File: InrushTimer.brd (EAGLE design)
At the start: 62.2 x 36 mm, 72 parts, among them IC1 TLC272D, IC2 555, IC3 4076N, Q1 TIP41C, Q2 TRANSISTOR-FET_2N7002, Q3 TRANSISTOR-FET_2N7002, Q4 TRANSISTOR-FET_2N7002, Q5 TRANSISTOR-FET_2N7002, T1 MMBTA05, U1 ROHM_BY_ELEMENT14_BATCH_1_BU4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

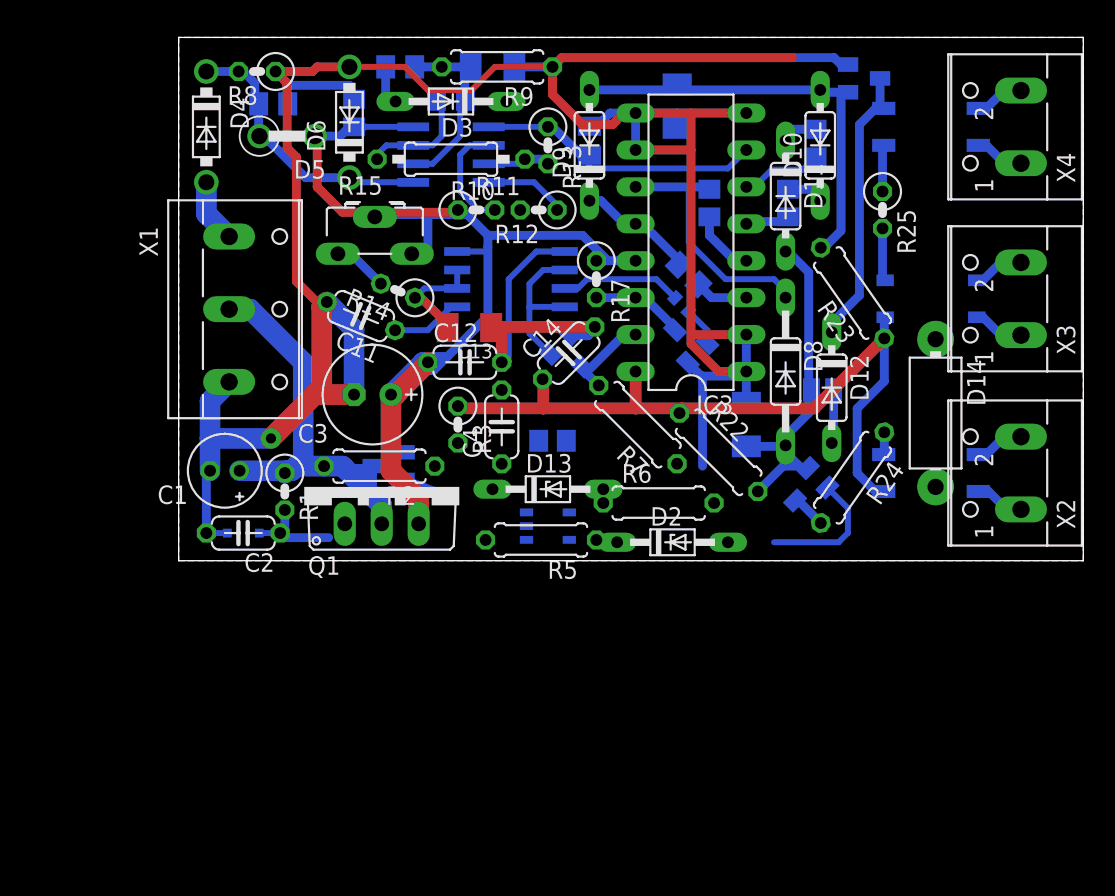
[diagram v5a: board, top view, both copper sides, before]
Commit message: Rerouted power supply section and made some space around the pot.
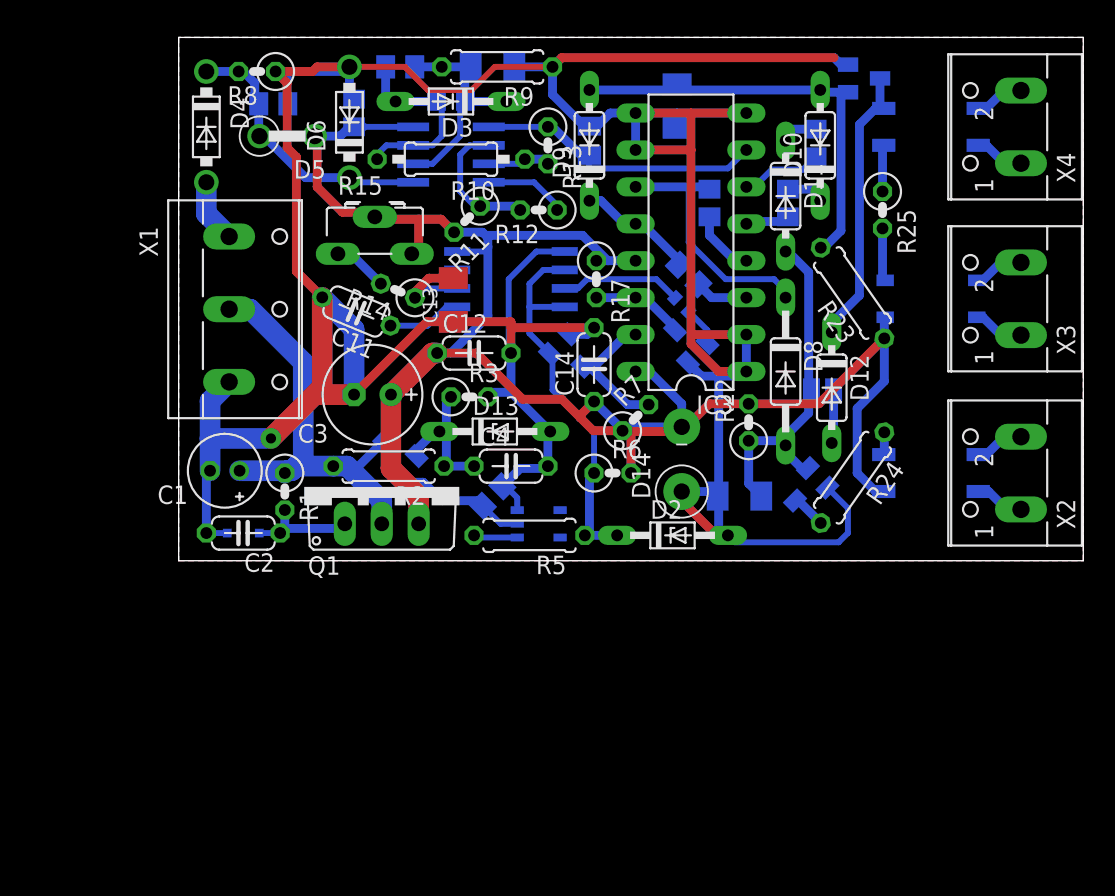
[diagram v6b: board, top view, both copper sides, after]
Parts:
- D14: value P6KEXXCTS-P6KE -> P6KEXXCDO15-10V; device diode:DO15-10 -> diode:DO15-10V
- R22, R6, R7: device rcl:0207/7 -> rcl:0207/2V
- moved D14 17.7 mm to (34.6, 6.99), turned to 90 degrees
- moved R4 5.62 mm to (21.6, 4.45), turned to 315 degrees
- moved D13 5.39 mm to (21.7, 8.89)
- moved C15 4.94 mm to (38.6, 4.45), turned to 180 degrees
- moved R6 3.79 mm to (29.8, 6.03)
- moved R22 2.92 mm to (39.2, 9.53), turned to 90 degrees
- moved C4 2.77 mm to (22.9, 6.51), turned to 0 degrees
- moved C13 2.21 mm to (18.9, 17.9), turned to 90 degrees
- moved R3 2.06 mm to (20.0, 11.3), turned to 0 degrees
- moved C14 1.92 mm to (28.6, 13.5), turned to 90 degrees
- moved T1 0.93 mm to (14.9, 7.30), turned to 315 degrees
- moved C12 0.90 mm to (20.3, 14.3)
- moved R11 0.90 mm to (19.8, 23.5), turned to 225 degrees
- moved R5 0.85 mm to (24.1, 1.75)
- moved U1 0.65 mm to (24.8, 2.54)
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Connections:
- net N$14: now also R3.1; no longer R3.2
- net ON_A_SYNC: now also R22.1; no longer R22.2
- net THRESH: now also R11.1; no longer R11.2
- net V12: now also D14.A, R11.2, R22.2; no longer D14.C, R11.1, R22.1
- net ZERO: now also D14.C, R3.2; no longer D14.A, R3.1
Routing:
- net ZERO: track 241.5 -> 278.8 mm
- net V12: track 130.8 -> 149.5 mm
- net RESET_N: track 10.7 -> 27.3 mm
- net N$14: track 0.00 -> 10.3 mm
- net N$13: track 3.08 -> 9.64 mm
- net RESET: track 6.30 -> 10.1 mm
- net N$23: track 0.00 -> 3.12 mm
- net THRESH: track 7.68 -> 9.58 mm
- net RECT: track 31.8 -> 30.0 mm
- net ON_A_SYNC: track 23.8 -> 24.6 mm
- net N$40: track 4.94 -> 5.55 mm
- net N$8: track 6.81 -> 7.42 mm

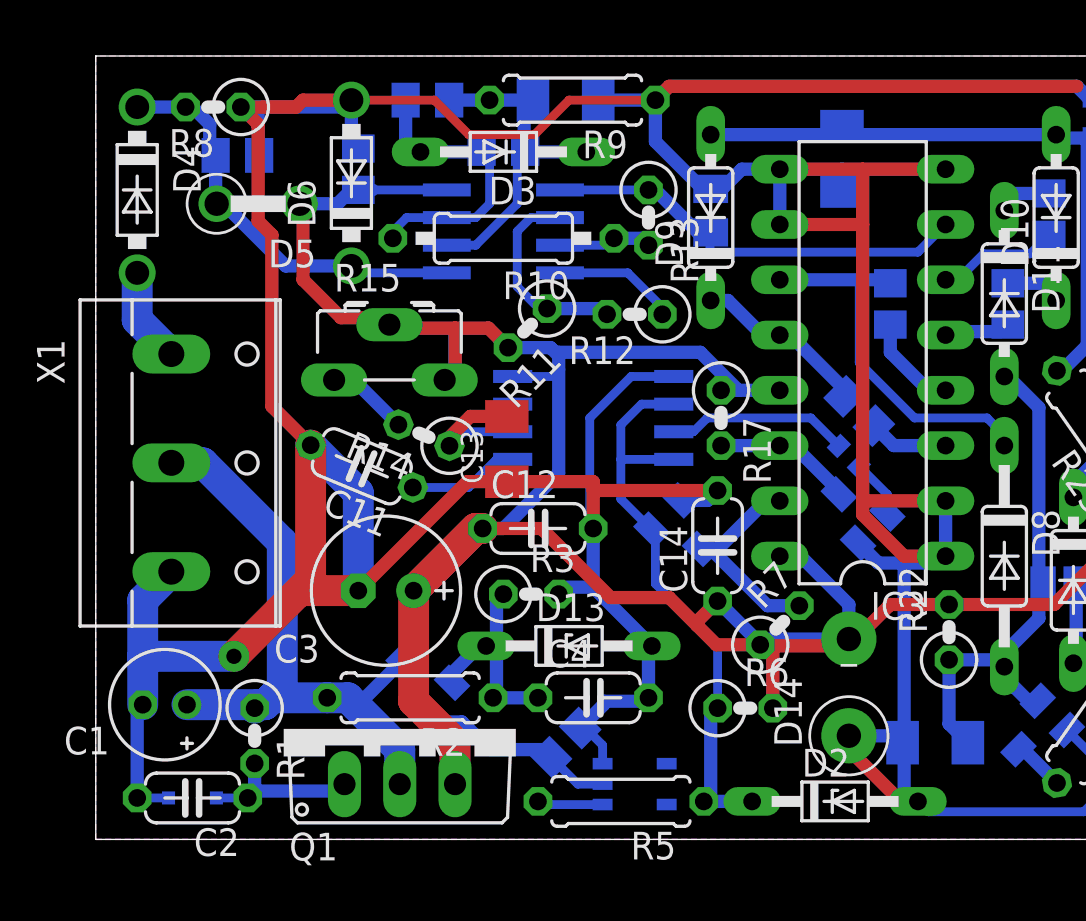
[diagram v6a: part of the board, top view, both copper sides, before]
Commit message: Fixed some component orientations.
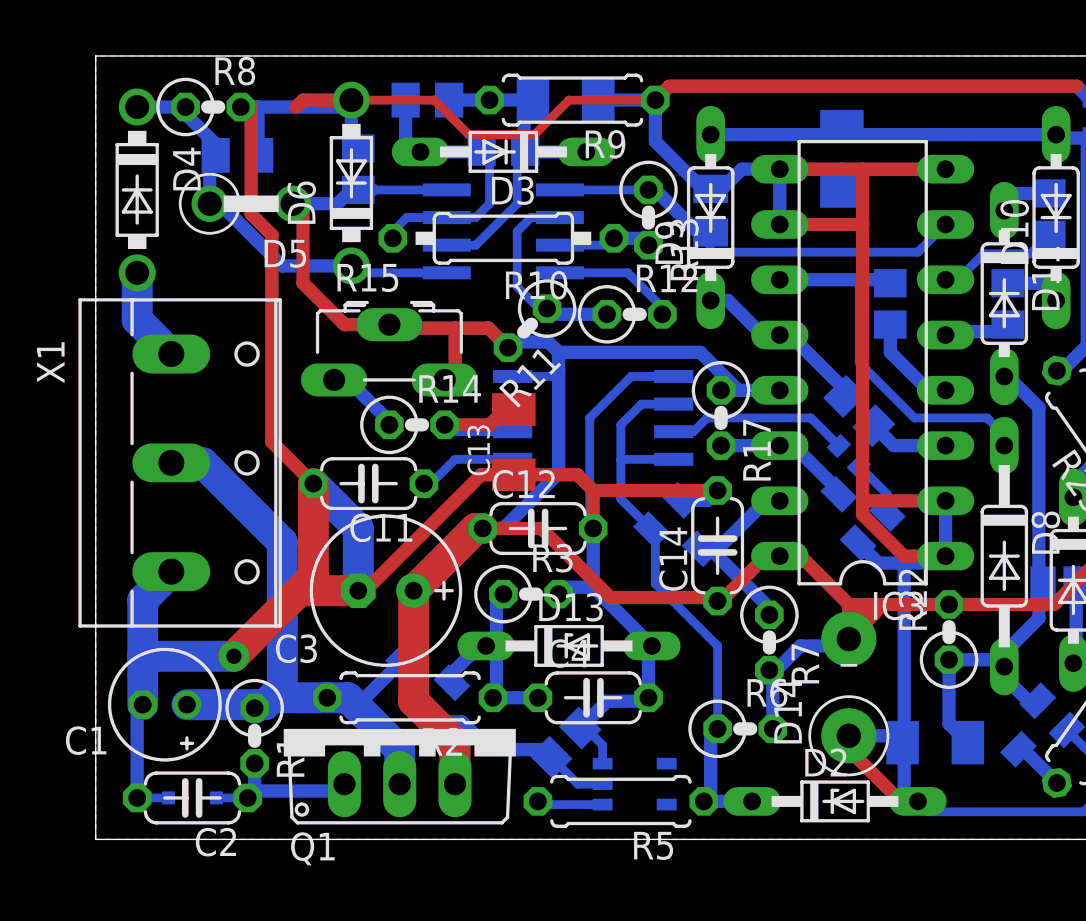
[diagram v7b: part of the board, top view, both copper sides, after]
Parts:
- moved R6 0.95 mm to (29.8, 5.08)
- moved R7 0.93 mm to (31.0, 9.05), turned to 270 degrees
- moved C11 0.85 mm to (12.5, 16.4), turned to 180 degrees
- moved R14 0.57 mm to (14.8, 19.1), turned to 0 degrees
- moved C13 0.45 mm to (19.2, 18.3)
- moved D5 0.32 mm to (7.14, 29.2)
- turned R12 to 0 degrees
- turned R8 to 0 degrees
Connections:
- removed net N$34: R14.2, R15.A
- new net N$2: R14.1, R15.A
- net N$11: now also R8.1; no longer R8.2
- net N$28: now also R14.2; no longer R14.1
- net RESET: now also R7.1; no longer R7.2
- net THRESH: now also R12.1; no longer R12.2
- net V12: now also R7.2; no longer R7.1
- net ZERO: now also R12.2, R8.2; no longer R12.1, R8.1
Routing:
- net N$34: track 3.80 -> 0.00 mm
- net ZERO: track 278.8 -> 275.2 mm
- net N$2: track 0.00 -> 3.49 mm
- net V12: track 149.5 -> 147.6 mm
- net N$40: track 5.55 -> 4.54 mm
- net RESET: track 10.1 -> 9.53 mm

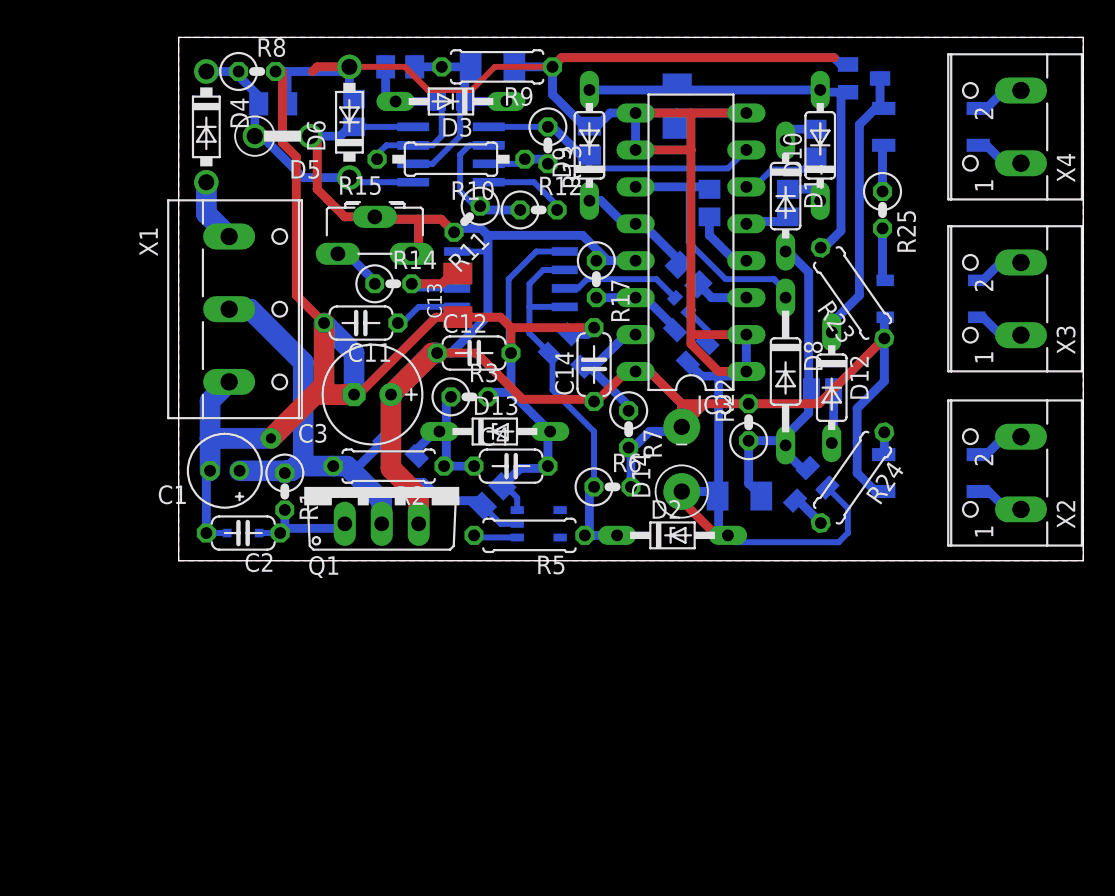
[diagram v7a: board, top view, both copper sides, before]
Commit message: Tweaked ground and component positions - still to do; adjust pad sizes.
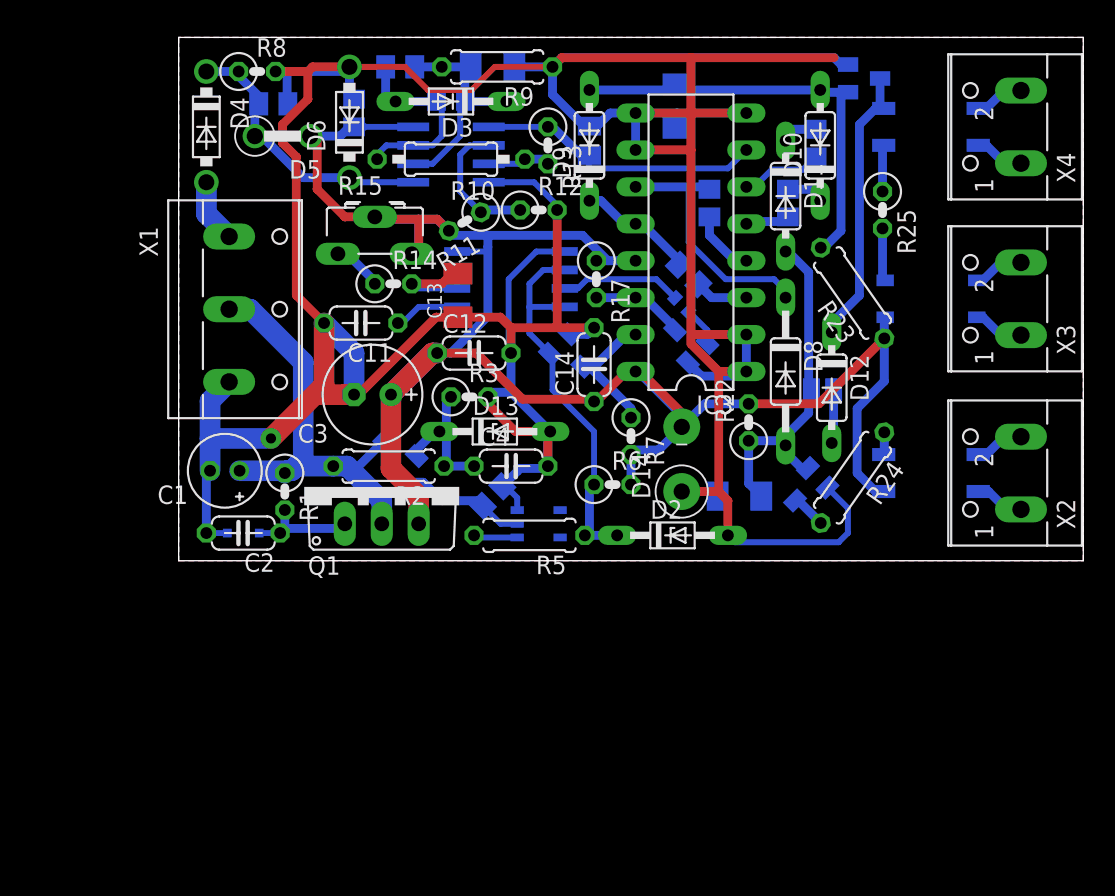
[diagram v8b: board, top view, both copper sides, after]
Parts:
- moved R7 0.50 mm to (31.1, 8.57)
- moved R11 0.22 mm to (19.7, 23.3), turned to 210 degrees
- moved R6 0.16 mm to (29.8, 5.24)
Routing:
- net ZERO: track 275.2 -> 296.5 mm
- net V12: track 147.6 -> 143.0 mm
- net RESET: track 9.53 -> 10.1 mm
